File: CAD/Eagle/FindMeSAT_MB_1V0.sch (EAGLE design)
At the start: 127 parts, among them IC1111 LM2831YMF, J291 MCX-J-P-X-RA-SM1, J685 SMA_CON, J701 MOLEX_105017-0001, J801 MICROSIM-8P_SDCARD-8P_MOLEX-1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, J901 JST_S3B-XH-A, Q101 ABS07, Q651 ABM3B-16MHZ-10-R50-1-U, U1001 CFPT-141, U101 ATXMEGA256A3BU-AU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

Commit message: Eagle - minor changes done
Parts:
- renumbered IC1111 to U1111
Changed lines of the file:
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@@
 <part name="FRAME10" library="df4iah_frame" deviceset="A4L-LOC" device="" value="BatteryConnector"/>
 <part name="FRAME11" library="df4iah_frame" deviceset="A4L-LOC" device="" value="Power"/>
-<part name="IC1111" library="df4iah_powersupply" deviceset="LM2831" device="" technology="YMF" value="LM2831YMF"/>
+<part name="U1111" library="df4iah_powersupply" deviceset="LM2831" device="" technology="YMF" value="LM2831YMF"/>
 <part name="+5V0_1111" library="df4iah_supply" deviceset="+5V" device=""/>
 <part name="C1111" library="rcl" deviceset="C-EU" device="C0805" value="47u"/>
@@
 <instances>
 <instance part="FRAME11" gate="G$1" x="0" y="0"/>
-<instance part="IC1111" gate="A" x="91.44" y="127" smashed="yes">
+<instance part="U1111" gate="A" x="91.44" y="127" smashed="yes">
 <attribute name="NAME" x="87.249" y="140.6906" size="2.0828" layer="95" ratio="10" rot="SR0"/>
 <attribute name="VALUE" x="84.5058" y="111.252" size="2.0828" layer="96" ratio="10" rot="SR0"/>
@@
 </segment>
 <segment>
-<pinref part="IC1111" gate="A" pin="GND"/>
+<pinref part="U1111" gate="A" pin="GND"/>
 <pinref part="GND1113" gate="1" pin="GND"/>
 <wire x1="109.22" y1="127" x2="127" y2="127" width="0.1524" layer="91"/>
@@
 <net name="EN" class="0">
 <segment>
-<pinref part="IC1111" gate="A" pin="EN"/>
+<pinref part="U1111" gate="A" pin="EN"/>
 <wire x1="73.66" y1="134.62" x2="63.5" y2="134.62" width="0.1524" layer="91"/>
 <wire x1="63.5" y1="134.62" x2="63.5" y2="132.08" width="0.1524" layer="91"/>
@@
 <pinref part="+5V0_1111" gate="G$1" pin="+5V"/>
 <wire x1="25.4" y1="149.86" x2="25.4" y2="137.16" width="0.1524" layer="91"/>
-<pinref part="IC1111" gate="A" pin="VIN"/>
+<pinref part="U1111" gate="A" pin="VIN"/>
 <wire x1="25.4" y1="137.16" x2="25.4" y2="119.38" width="0.1524" layer="91"/>
 <wire x1="73.66" y1="119.38" x2="63.5" y2="119.38" width="0.1524" layer="91"/>
@@
 <net name="SW" class="0">
 <segment>
-<pinref part="IC1111" gate="A" pin="SW"/>
+<pinref part="U1111" gate="A" pin="SW"/>
 <wire x1="109.22" y1="119.38" x2="127" y2="119.38" width="0.1524" layer="91"/>
 <pinref part="D1111" gate="G$1" pin="C"/>
@@
 <wire x1="218.44" y1="104.14" x2="210.82" y2="104.14" width="0.1524" layer="91"/>
 <wire x1="210.82" y1="104.14" x2="210.82" y2="134.62" width="0.1524" layer="91"/>
-<pinref part="IC1111" gate="A" pin="FB"/>
+<pinref part="U1111" gate="A" pin="FB"/>
 <wire x1="210.82" y1="134.62" x2="109.22" y2="134.62" width="0.1524" layer="91"/>
 <junction x="218.44" y="104.14"/>

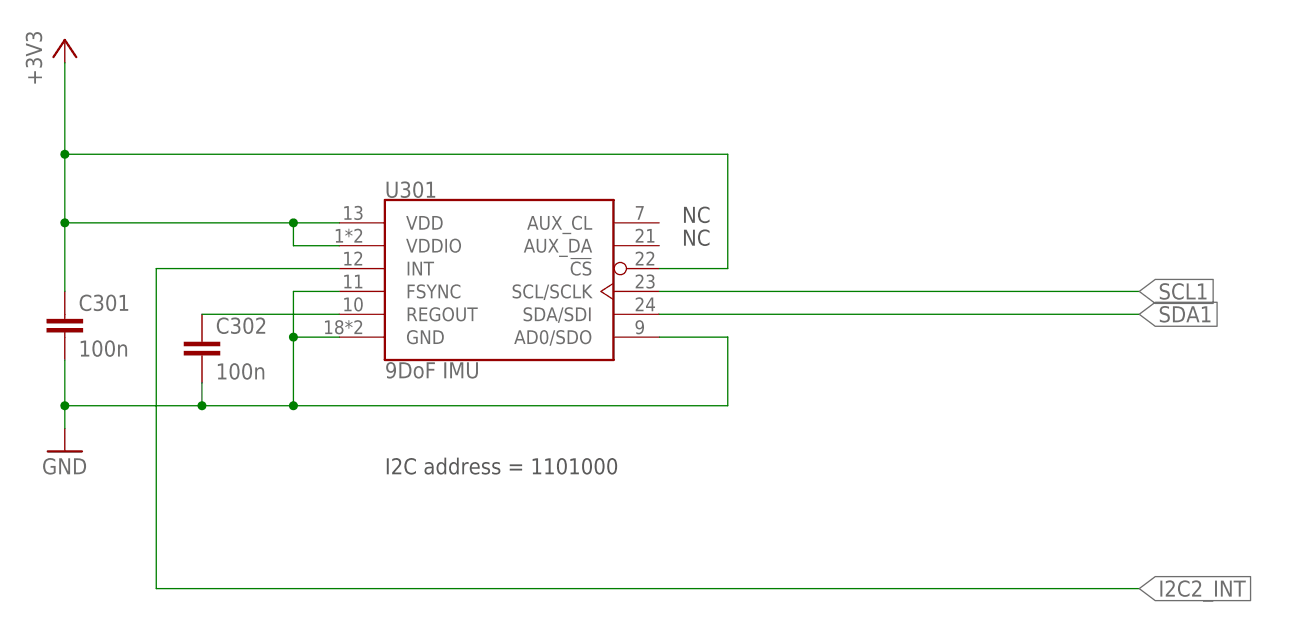
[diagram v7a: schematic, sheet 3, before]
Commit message: Eagle - values corrected and placed
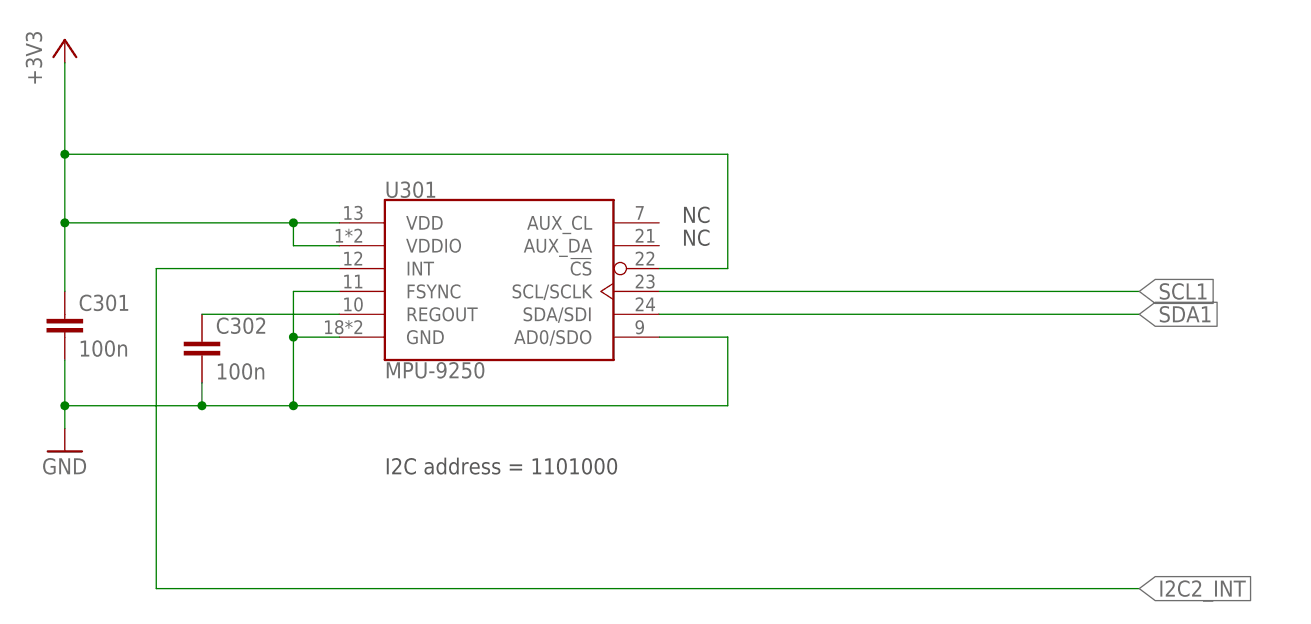
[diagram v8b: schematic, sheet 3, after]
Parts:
- JP111: value JTAG -> AVR-JTAG-10
- JP121: value DISPLAY -> HEADER-2X3
- JP131: value PDI -> HEADER-2X3
- U301: value 9DoF IMU -> MPU-9250
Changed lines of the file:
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@@
 <part name="R132" library="rcl" deviceset="R-EU_" device="R0603" value="27"/>
 <part name="R112" library="rcl" deviceset="R-EU_" device="R0603" value="10k"/>
-<part name="JP131" library="df4iah_connector" deviceset="HEADER-2X3" device="" value="PDI"/>
+<part name="JP131" library="df4iah_connector" deviceset="HEADER-2X3" device="" value=""/>
 <part name="GND131" library="df4iah_supply" deviceset="GND" device=""/>
 <part name="R1002" library="rcl" deviceset="R-EU_" device="R0603" value="10k"/>
-<part name="JP111" library="df4iah_connector" deviceset="AVR-JTAG-10" device="" value="JTAG"/>
+<part name="JP111" library="df4iah_connector" deviceset="AVR-JTAG-10" device="" value=""/>
 <part name="GND111" library="df4iah_supply" deviceset="GND" device=""/>
 <part name="R111" library="rcl" deviceset="R-EU_" device="R0805" value="150"/>
@@
 <part name="C141" library="rcl" deviceset="C-EU" device="C0603" value="100p"/>
 <part name="GND141" library="df4iah_supply" deviceset="GND" device=""/>
-<part name="JP121" library="df4iah_connector" deviceset="HEADER-2X3" device="" value="DISPLAY"/>
+<part name="JP121" library="df4iah_connector" deviceset="HEADER-2X3" device="" value=""/>
 <part name="GND121" library="df4iah_supply" deviceset="GND" device=""/>
 <part name="+5V1" library="df4iah_supply" deviceset="+5V" device=""/>
-<part name="U301" library="df4iah_sensors" deviceset="MPU-9250" device="" value="9DoF IMU"/>
+<part name="U301" library="df4iah_sensors" deviceset="MPU-9250" device="" value="MPU-9250"/>
 <part name="GND311" library="df4iah_supply" deviceset="GND" device=""/>
 <part name="+3V3_311" library="df4iah_supply" deviceset="+3V3" device=""/>
